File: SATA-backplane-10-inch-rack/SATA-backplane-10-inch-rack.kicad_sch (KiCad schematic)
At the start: 9 parts, among them J101 67800-5001, J102 1735284-2, J103 Barrel_Jack_Switch_Pin3Ring, U101 HW-613 5V0, U102 HW-613 3V3

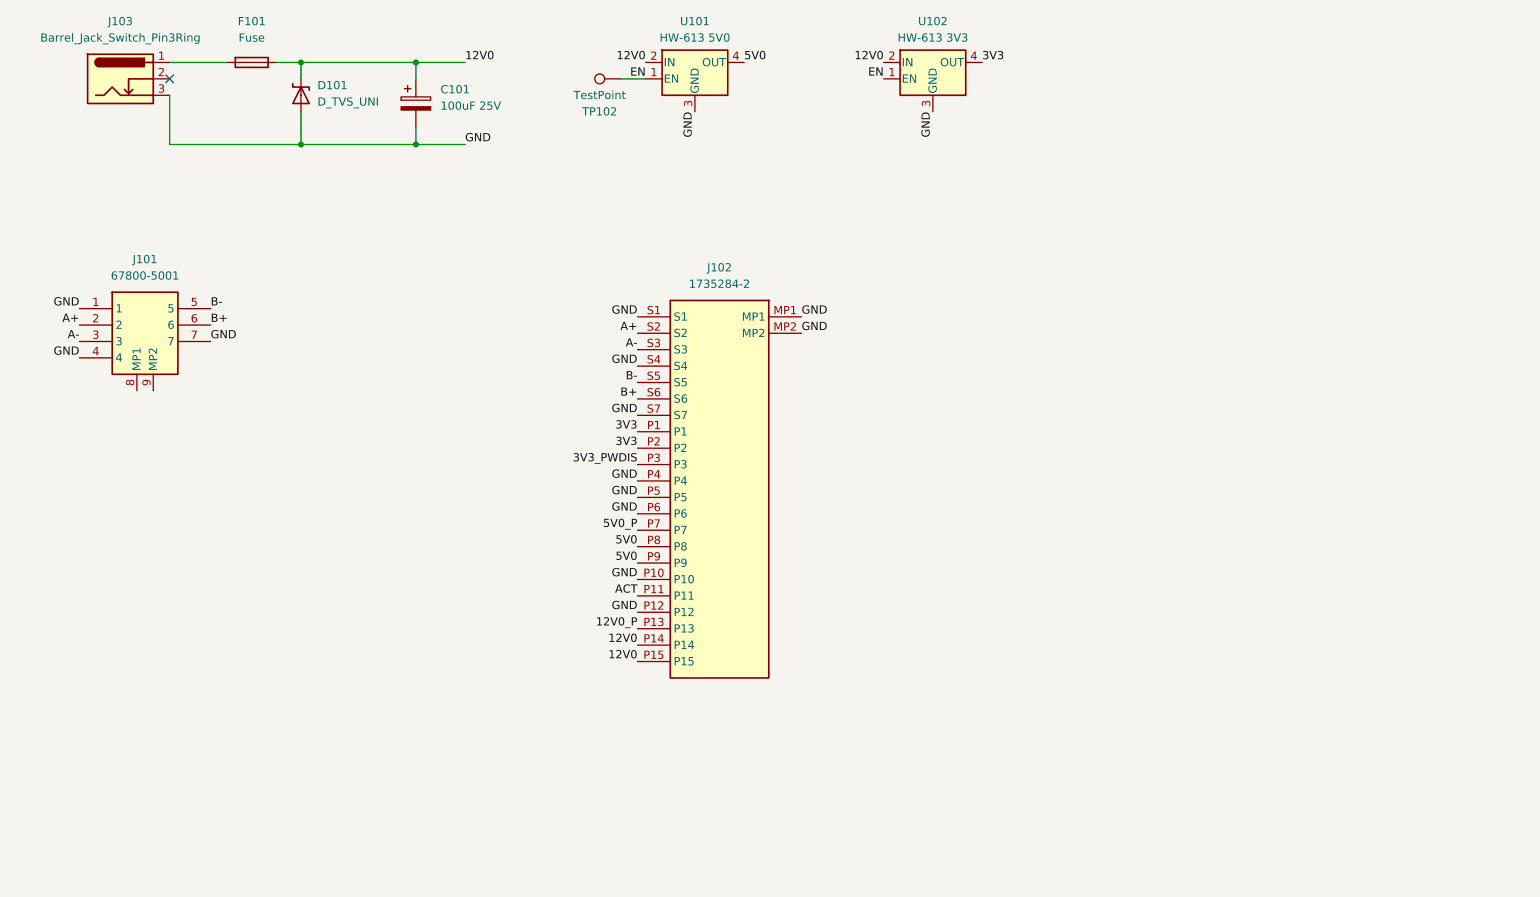
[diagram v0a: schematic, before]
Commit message: Draw 12-module layout example
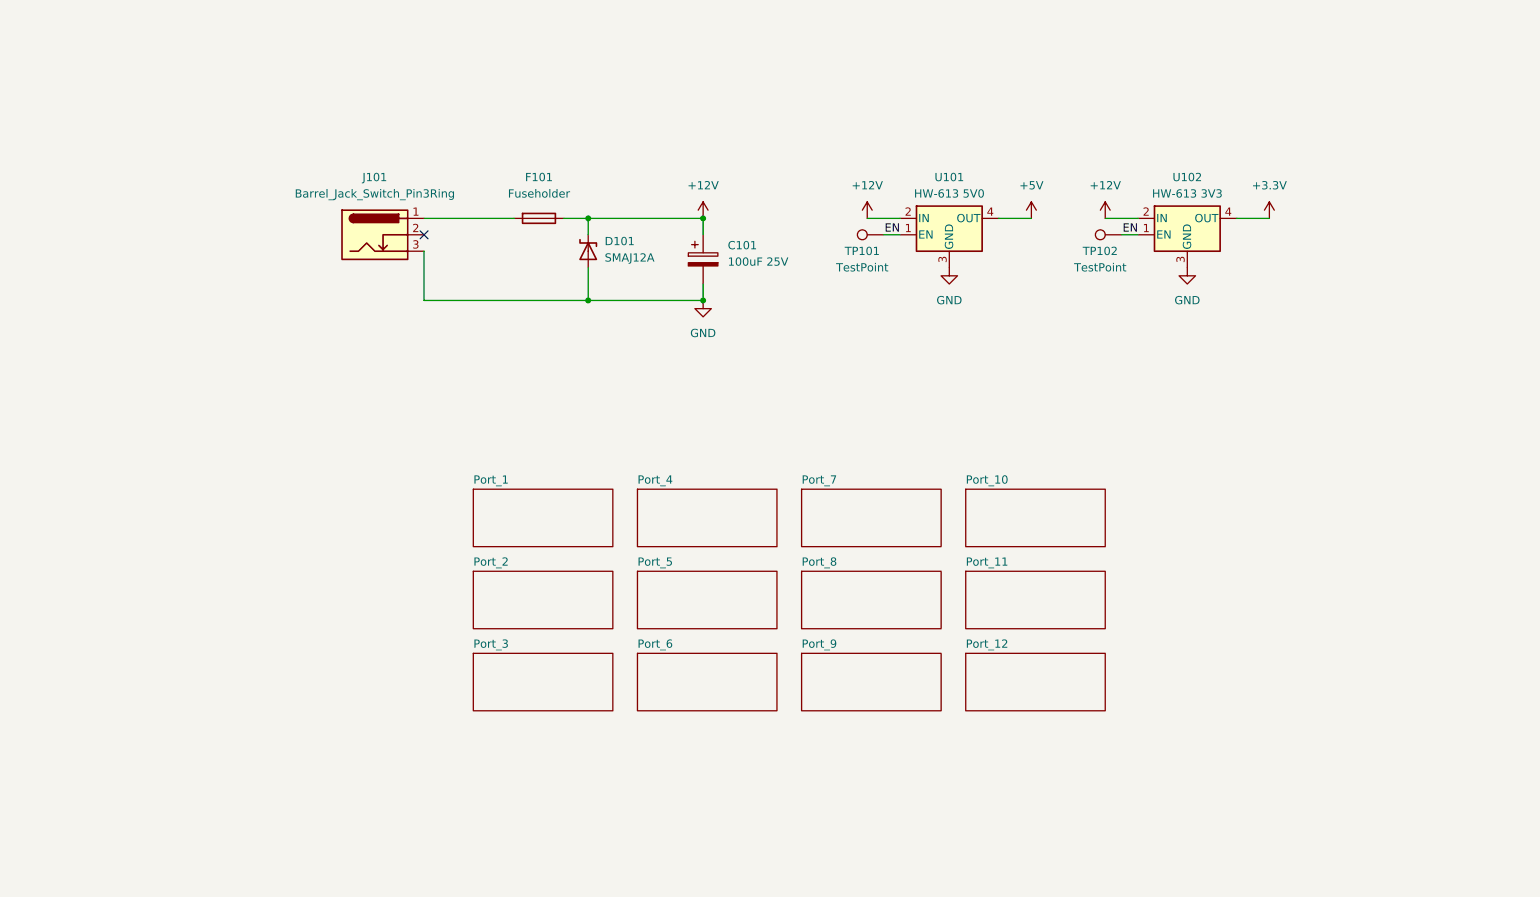
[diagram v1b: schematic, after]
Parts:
- removed J101: 67800-5001, Libraries:67800-5005_2, symbol 67800-5001:67800-5001
- removed J102: 1735284-2, Libraries:17352842, symbol 1735284-2:1735284-2
- removed J103: Barrel_Jack_Switch_Pin3Ring, Connector_BarrelJack:BarrelJack_CUI_PJ-036AH-SMT_Horizontal, symbol Connector:Barrel_Jack_Switch_Pin3Ring
- added J101: Barrel_Jack_Switch_Pin3Ring, Libraries:PJ036AHSMTTR, symbol Connector:Barrel_Jack_Switch_Pin3Ring
- added TP101: TestPoint, TestPoint:TestPoint_Pad_D1.5mm, symbol Connector:TestPoint
- D101: value D_TVS_UNI -> SMAJ12A
- F101: value Fuse -> Fuseholder; footprint Fuse:Fuseholder_Cylinder-5x20mm_Wuerth_696103101002-SMD_Horizontal_Open -> Libraries:Fuseholder_Cylinder-5x20mm_Wuerth_696103101002-SMD_Horizontal_Open
- TP102: footprint TestPoint:TestPoint_Pad_D3.0mm -> TestPoint:TestPoint_Pad_D1.5mm
- U101, U102: footprint Connector_PinHeader_2.54mm:PinHeader_1x04_P2.54mm_Vertical_SMD_Pin1Right -> Libraries:HW-613
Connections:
- net EN: now also TP101.1
- net GND: now also J101.3
- net at F101.2: now also J101.1
- net 12V0 renamed +12V
- net 3V3 renamed +3.3V
- net 5V0 renamed +5V
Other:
- added sheet Port_1 (Port.kicad_sch)
- added sheet Port_10 (Port.kicad_sch)
- added sheet Port_11 (Port.kicad_sch)
- added sheet Port_12 (Port.kicad_sch)
- added sheet Port_2 (Port.kicad_sch)
- added sheet Port_3 (Port.kicad_sch)
- added sheet Port_4 (Port.kicad_sch)
- added sheet Port_5 (Port.kicad_sch)
- added sheet Port_6 (Port.kicad_sch)
- added sheet Port_7 (Port.kicad_sch)
- added sheet Port_8 (Port.kicad_sch)
- added sheet Port_9 (Port.kicad_sch)

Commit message: More realistic layout
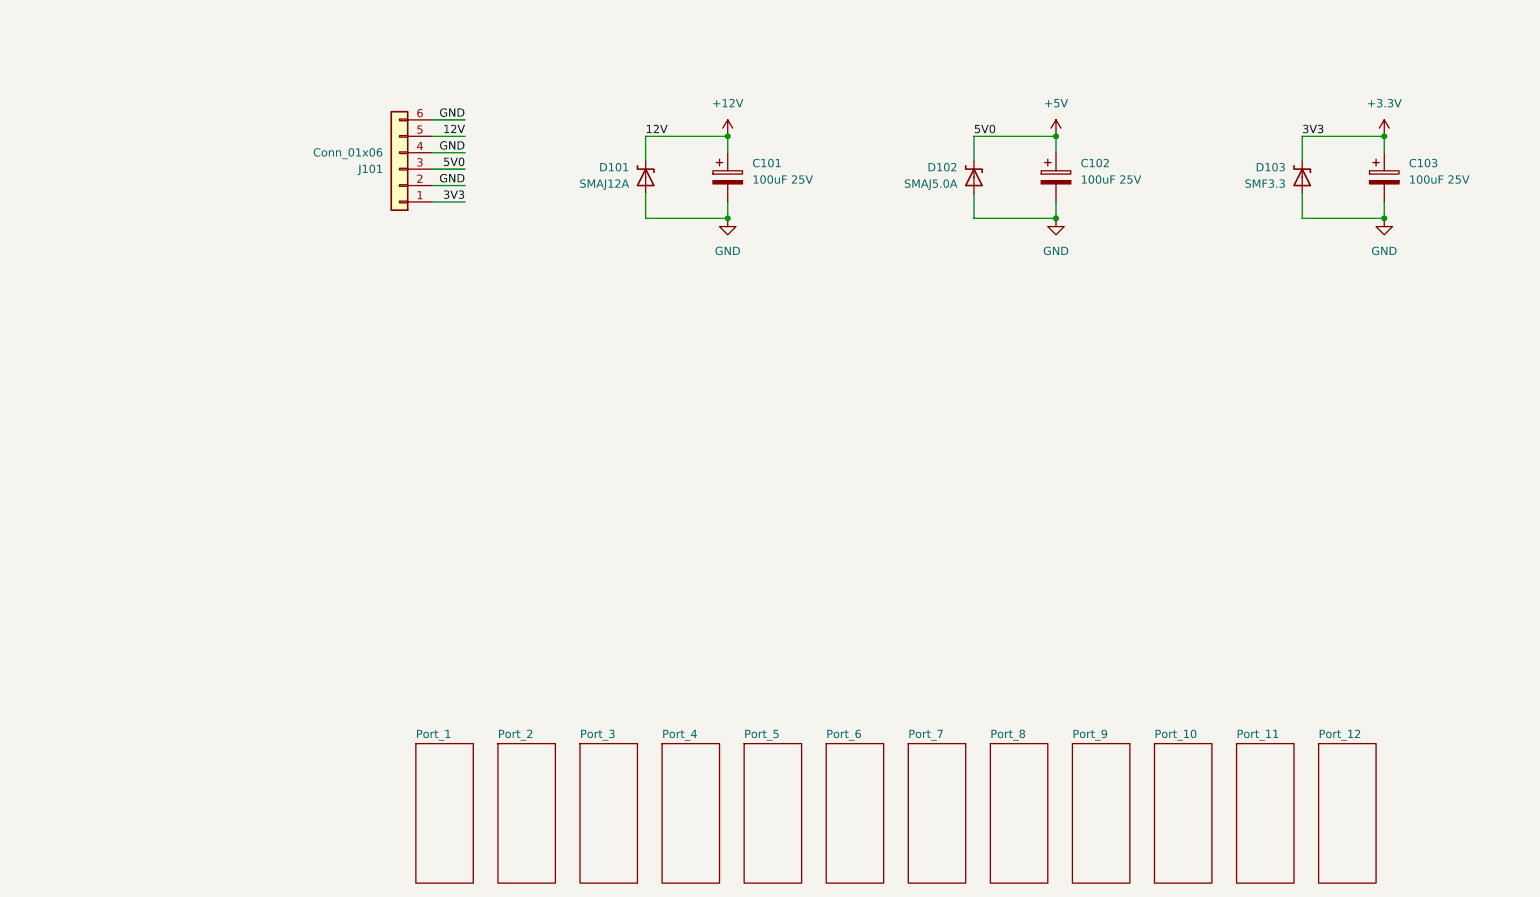
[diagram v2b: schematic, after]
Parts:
- removed F101: Fuseholder, Libraries:Fuseholder_Cylinder-5x20mm_Wuerth_696103101002-SMD_Horizontal_Open, symbol Device:Fuse
- removed J101: Barrel_Jack_Switch_Pin3Ring, Libraries:PJ036AHSMTTR, symbol Connector:Barrel_Jack_Switch_Pin3Ring
- removed TP101, TP102: TestPoint, TestPoint:TestPoint_Pad_D1.5mm, symbol Connector:TestPoint
- removed U101: HW-613 5V0, Libraries:HW-613, symbol HW-613:HW-613
- removed U102: HW-613 3V3, Libraries:HW-613, symbol HW-613:HW-613
- added C102, C103: 100uF 25V, Capacitor_SMD:CP_Elec_8x10.5, symbol Device:C_Polarized
- added D102: SMAJ5.0A, Diode_SMD:D_SMA-SMB_Universal_Handsoldering, symbol Kharars-KiCAD-lib:D_TVS_UNI
- added D103: SMF3.3, Diode_SMD:D_SMA-SMB_Universal_Handsoldering, symbol Kharars-KiCAD-lib:D_TVS_UNI
- added J101: Conn_01x06, TerminalBlock_Phoenix_PT-1,5-6-3.5-H_1x06_P3.50mm_Horizontal, symbol Connector_Generic:Conn_01x06
- C101: Manufacturer_Name (none) -> Panasonic; Manufacturer_Part_Number (none) -> EEE-HC1E101P
- D101: Manufacturer_Name (none) -> Bourns; Manufacturer_Part_Number (none) -> SMAJ12A
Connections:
- net +12V: now also J101.5 (Pin_5)
- net +3.3V: now also C103.1, D103.1 (A1), J101.1 (Pin_1)
- net +5V: now also C102.1, D102.1 (A1), J101.3 (Pin_3)
- net GND: now also C102.2, C103.2, D102.2 (A2), D103.2 (A2), J101.2 (Pin_2), J101.4 (Pin_4), J101.6 (Pin_6)
- no-connect marks 1 -> 0

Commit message: STA/ACT implemented in layout
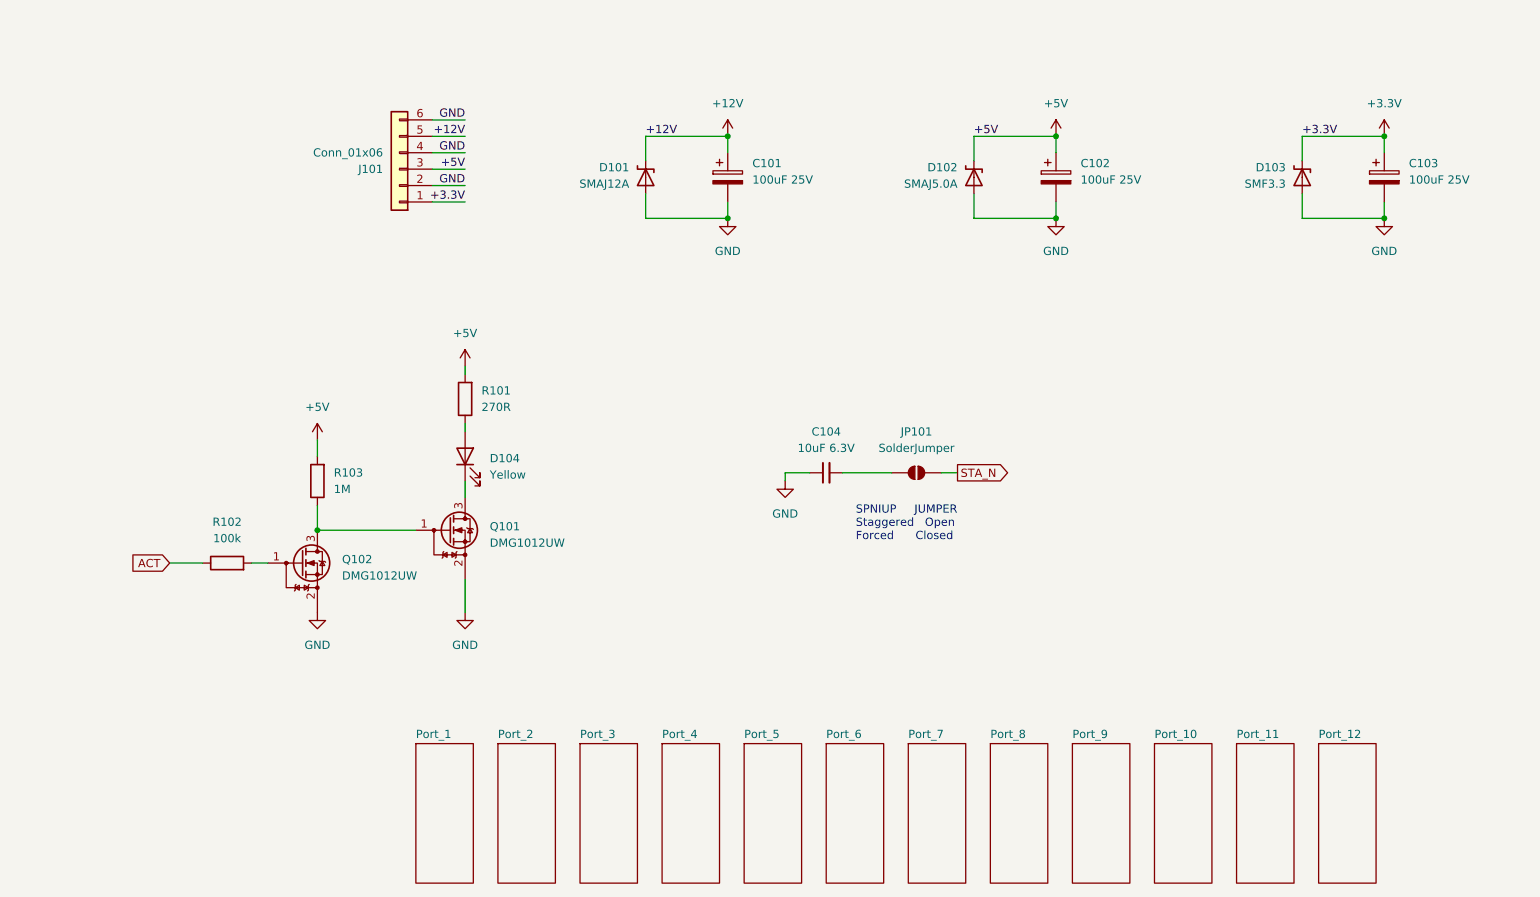
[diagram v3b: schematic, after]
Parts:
- added C104: 10uF 6.3V, Capacitor_SMD:C_0805_2012Metric_Pad1.18x1.45mm_HandSolder, symbol Device:C_Small
- added D104: Yellow, LED_SMD:LED_0805_2012Metric_Pad1.15x1.40mm_HandSolder, symbol Device:LED
- added JP101: SolderJumper, Jumper:SolderJumper-2_P1.3mm_Open_RoundedPad1.0x1.5mm, symbol Jumper:SolderJumper_2_Open
- added Q101, Q102: DMG1012UW, Package_TO_SOT_SMD:SOT-323_SC-70, symbol Kharars-KiCAD-lib:DMG1012UW
- added R101: 270R, Resistor_SMD:R_0805_2012Metric_Pad1.20x1.40mm_HandSolder, symbol Device:R
- added R102: 100k, Resistor_SMD:R_0805_2012Metric_Pad1.20x1.40mm_HandSolder, symbol Device:R
- added R103: 1M, Resistor_SMD:R_0805_2012Metric_Pad1.20x1.40mm_HandSolder, symbol Device:R
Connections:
- net +5V: now also R101.2, R103.2
- net GND: now also C104.1, Q101.2 (S), Q102.2 (S)
- new net: D104.2 (A), R101.1
- new net: Q101.1 (G), Q102.3 (D), R103.1
- new net: D104.1 (K), Q101.3 (D)
- new net: C104.2, JP101.1 (A)
- new net: Q102.1 (G), R102.2
- new net ACT: R102.1
- new net STA_N: JP101.2 (B)
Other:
- note added: "SPNIUP JUMPER Staggered Open Forced Closed"
